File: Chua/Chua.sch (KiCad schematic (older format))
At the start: 18 parts, among them U1 TL082, U2 TL082

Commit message: assigned R and C footprint
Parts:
- C1, C2, C3: footprint (none) -> Capacitors_SMD:C_0805_HandSoldering
- R1, R2, R3, R4, R5, R6, R7, R8, R9: footprint (none) -> Resistors_SMD:R_0805_HandSoldering
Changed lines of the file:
@@
 F 0 "U2" H 9150 2550 50  0000 L CNN
 F 1 "TL082" H 9150 2150 50  0000 L CNN
-F 2 "" H 9150 2350 50  0000 C CNN
+F 2 "" H 9150 2350 50  0001 C CNN
 F 3 "" H 9150 2350 50  0000 C CNN
 	2    9150 2350
@@
 F 0 "U2" H 7900 2550 50  0000 L CNN
 F 1 "TL082" H 7900 2150 50  0000 L CNN
-F 2 "" H 7900 2350 50  0000 C CNN
+F 2 "" H 7900 2350 50  0001 C CNN
 F 3 "" H 7900 2350 50  0000 C CNN
 	1    7900 2350
@@
 F 0 "U1" H 4400 2700 50  0000 L CNN
 F 1 "TL082" H 4400 2300 50  0000 L CNN
-F 2 "" H 4400 2500 50  0000 C CNN
+F 2 "" H 4400 2500 50  0001 C CNN
 F 3 "" H 4400 2500 50  0000 C CNN
 	1    4400 2500
@@
 F 0 "U1" H 5800 3850 50  0000 L CNN
 F 1 "TL082" H 5800 3450 50  0000 L CNN
-F 2 "" H 5800 3650 50  0000 C CNN
+F 2 "" H 5800 3650 50  0001 C CNN
 F 3 "" H 5800 3650 50  0000 C CNN
 	2    5800 3650
@@
 F 0 "R4" V 8130 1850 50  0000 C CNN
 F 1 "R" V 8050 1850 50  0000 C CNN
-F 2 "" V 7980 1850 50  0000 C CNN
+F 2 "Resistors_SMD:R_0805_HandSoldering" V 7980 1850 50  0001 C CNN
 F 3 "" H 8050 1850 50  0000 C CNN
 	1    8050 1850
@@
 F 0 "R8" V 9080 1850 50  0000 C CNN
 F 1 "R" V 9000 1850 50  0000 C CNN
-F 2 "" V 8930 1850 50  0000 C CNN
+F 2 "Resistors_SMD:R_0805_HandSoldering" V 8930 1850 50  0001 C CNN
 F 3 "" H 9000 1850 50  0000 C CNN
 	1    9000 1850
@@
 F 0 "R5" V 8130 2850 50  0000 C CNN
 F 1 "R" V 8050 2850 50  0000 C CNN
-F 2 "" V 7980 2850 50  0000 C CNN
+F 2 "Resistors_SMD:R_0805_HandSoldering" V 7980 2850 50  0001 C CNN
 F 3 "" H 8050 2850 50  0000 C CNN
 	1    8050 2850
@@
 F 0 "R9" V 9130 2850 50  0000 C CNN
 F 1 "R" V 9050 2850 50  0000 C CNN
-F 2 "" V 8980 2850 50  0000 C CNN
+F 2 "Resistors_SMD:R_0805_HandSoldering" V 8980 2850 50  0001 C CNN
 F 3 "" H 9050 2850 50  0000 C CNN
 	1    9050 2850
@@
 F 0 "R6" V 8430 3200 50  0000 C CNN
 F 1 "R" V 8350 3200 50  0000 C CNN
-F 2 "" V 8280 3200 50  0000 C CNN
+F 2 "Resistors_SMD:R_0805_HandSoldering" V 8280 3200 50  0001 C CNN
 F 3 "" H 8350 3200 50  0000 C CNN
 	1    8350 3200
@@
 F 0 "R7" V 8880 3200 50  0000 C CNN
 F 1 "R" V 8800 3200 50  0000 C CNN
-F 2 "" V 8730 3200 50  0000 C CNN
+F 2 "Resistors_SMD:R_0805_HandSoldering" V 8730 3200 50  0001 C CNN
 F 3 "" H 8800 3200 50  0000 C CNN
 	1    8800 3200
@@
 F 0 "R2" V 5180 2700 50  0000 C CNN
 F 1 "R" V 5100 2700 50  0000 C CNN
-F 2 "" V 5030 2700 50  0000 C CNN
+F 2 "Resistors_SMD:R_0805_HandSoldering" V 5030 2700 50  0001 C CNN
 F 3 "" H 5100 2700 50  0000 C CNN
 	1    5100 2700
@@
 F 0 "R1" V 5180 2300 50  0000 C CNN
 F 1 "R" V 5100 2300 50  0000 C CNN
-F 2 "" V 5030 2300 50  0000 C CNN
+F 2 "Resistors_SMD:R_0805_HandSoldering" V 5030 2300 50  0001 C CNN
 F 3 "" H 5100 2300 50  0000 C CNN
 	1    5100 2300
@@
 F 0 "R3" V 5180 3450 50  0000 C CNN
 F 1 "R" V 5100 3450 50  0000 C CNN
-F 2 "" V 5030 3450 50  0000 C CNN
+F 2 "Resistors_SMD:R_0805_HandSoldering" V 5030 3450 50  0001 C CNN
 F 3 "" H 5100 3450 50  0000 C CNN
 	1    5100 3450
@@
 F 0 "RV1" H 5650 4670 50  0000 C CNN
 F 1 "POT" H 5650 4750 50  0000 C CNN
-F 2 "" H 5650 4750 50  0000 C CNN
+F 2 "" H 5650 4750 50  0001 C CNN
 F 3 "" H 5650 4750 50  0000 C CNN
 	1    5650 4750
@@
 F 0 "RV2" H 6650 1770 50  0000 C CNN
 F 1 "POT" H 6650 1850 50  0000 C CNN
-F 2 "" H 6650 1850 50  0000 C CNN
+F 2 "" H 6650 1850 50  0001 C CNN
 F 3 "" H 6650 1850 50  0000 C CNN
 	1    6650 1850
@@
 F 0 "C3" H 6925 2550 50  0000 L CNN
 F 1 "C" H 6925 2350 50  0000 L CNN
-F 2 "" H 6938 2300 50  0000 C CNN
+F 2 "Capacitors_SMD:C_0805_HandSoldering" H 6938 2300 50  0001 C CNN
 F 3 "" H 6900 2450 50  0000 C CNN
 	1    6900 2450
@@
 F 0 "C2" H 6325 2550 50  0000 L CNN
 F 1 "C" H 6325 2350 50  0000 L CNN
-F 2 "" H 6338 2300 50  0000 C CNN
+F 2 "Capacitors_SMD:C_0805_HandSoldering" H 6338 2300 50  0001 C CNN
 F 3 "" H 6300 2450 50  0000 C CNN
 	1    6300 2450
@@
 F 0 "C1" H 5125 4000 50  0000 L CNN
 F 1 "C" H 5125 3800 50  0000 L CNN
-F 2 "" H 5138 3750 50  0000 C CNN
+F 2 "Capacitors_SMD:C_0805_HandSoldering" H 5138 3750 50  0001 C CNN
 F 3 "" H 5100 3900 50  0000 C CNN
 	1    5100 3900
@@
 F 0 "BT1" H 3150 3000 50  0000 L CNN
 F 1 "Battery" H 3150 2900 50  0000 L CNN
-F 2 "" V 3050 2990 50  0000 C CNN
+F 2 "" V 3050 2990 50  0001 C CNN
 F 3 "" V 3050 2990 50  0000 C CNN
 	1    3050 2950
@@
 F 0 "BT2" H 3150 3450 50  0000 L CNN
 F 1 "Battery" H 3150 3350 50  0000 L CNN
-F 2 "" V 3050 3440 50  0000 C CNN
+F 2 "" V 3050 3440 50  0001 C CNN
 F 3 "" V 3050 3440 50  0000 C CNN
 	1    3050 3400

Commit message: something
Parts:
- removed BT1, BT2: Battery, symbol Battery
- added P1: CONN_01X03, symbol CONN_01X03
- RV1, RV2: symbol POT -> POT-RESCUE-Chua
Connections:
- wire segments 57 -> 58
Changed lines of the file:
@@
 EESchema Schematic File Version 2
+LIBS:Chua-rescue
 LIBS:power
 LIBS:device
@@
 $EndComp
 $Comp
-L POT RV1
+L POT-RESCUE-Chua RV1
 U 1 1 588EAC9A
 P 5650 4750
@@
 $EndComp
 $Comp
-L POT RV2
+L POT-RESCUE-Chua RV2
 U 1 1 588EB185
 P 6650 1850
@@
 F 3 "" H 6600 4350 50  0000 C CNN
 	1    6600 4350
-	1    0    0    -1
-$EndComp
-$Comp
-L Battery BT1
-U 1 1 588EDD7C
-P 3050 2950
-F 0 "BT1" H 3150 3000 50  0000 L CNN
-F 1 "Battery" H 3150 2900 50  0000 L CNN
-F 2 "" V 3050 2990 50  0001 C CNN
-F 3 "" V 3050 2990 50  0000 C CNN
-	1    3050 2950
-	1    0    0    -1
-$EndComp
-$Comp
-L Battery BT2
-U 1 1 588EDE8E
-P 3050 3400
-F 0 "BT2" H 3150 3450 50  0000 L CNN
-F 1 "Battery" H 3150 3350 50  0000 L CNN
-F 2 "" V 3050 3440 50  0001 C CNN
-F 3 "" V 3050 3440 50  0000 C CNN
-	1    3050 3400
 	1    0    0    -1
 $EndComp
@@
 	6900 1850 7900 1850
 Wire Wire Line
-	3050 3250 3050 3100
-Wire Wire Line
-	3050 2800 3050 2450
-Wire Wire Line
-	3700 3200 3050 3200
-Connection ~ 3050 3200
-Wire Wire Line
-	3050 3950 3050 3550
+	3050 2450 3050 3100
+Wire Wire Line
+	2900 3200 3700 3200
+Wire Wire Line
+	3050 3300 3050 3950
 Text Label 3350 2450 0    60   ~ 0
 VCC+
 Text Label 3450 3950 0    60   ~ 0
 VCC-
+Entry Wire Line
+	5700 3800 5800 3900
+$Comp
+L CONN_01X03 P1
+U 1 1 5912531E
+P 2700 3200
+F 0 "P1" H 2700 3400 50  0000 C CNN
+F 1 "CONN_01X03" V 2800 3200 50  0000 C CNN
+F 2 "" H 2700 3200 50  0000 C CNN
+F 3 "" H 2700 3200 50  0000 C CNN
+	1    2700 3200
+	-1   0    0    1
+$EndComp
+Wire Wire Line
+	3050 3100 2900 3100
+Wire Wire Line
+	3050 3300 2900 3300
 $EndSCHEMATC

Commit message: update
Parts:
- added BT1, BT2: Battery_Cell, DM_Custom:DM_9V_ON_BOARD, symbol Battery_Cell
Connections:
- net GND: now also BT1.2 (-), BT2.1 (+)
- net VCC+: now also BT1.1 (+)
- net VCC-: now also BT2.2 (-)
- net at R4.1, R8.2, U2.5 (+): now also U2.3 (+); no longer U2.2 (-)
- net at R5.1, R6.1: now also U2.2 (-); no longer U2.3 (+)
- net at C2.1, R1.1, RV2.1: now also U1.3 (+); no longer U1.2 (-)
- net at R2.2, R3.1: now also U1.2 (-), U1.6 (-); no longer U1.3 (+), U1.5 (+)
- net at C1.2, RV1.2: now also U1.5 (+); no longer U1.6 (-)
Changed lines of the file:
@@
 Connection ~ 8700 1850
 Wire Wire Line
-	8200 2250 8450 2250
-Wire Wire Line
-	8450 2250 8450 1850
+	8450 1850 8450 2450
 Connection ~ 8450 1850
 Wire Wire Line
@@
 Connection ~ 7500 2350
 Wire Wire Line
-	8350 3050 8350 2450
-Wire Wire Line
-	8350 2450 8200 2450
+	8350 2250 8350 3050
 Wire Wire Line
 	8200 2850 8350 2850
@@
 	6100 2500 5100 2500
 Connection ~ 5100 2500
-Wire Wire Line
-	4700 2400 4700 2050
-Wire Wire Line
-	4700 2050 5100 2050
 Connection ~ 5100 2050
-Wire Wire Line
-	4700 2600 4700 2950
-Wire Wire Line
-	4700 2950 5100 2950
 Wire Wire Line
 	5100 2850 5100 3300
@@
 	4100 3650 5100 3650
 Connection ~ 5100 3650
-Wire Wire Line
-	5500 3750 5500 4200
-Wire Wire Line
-	5500 4200 5100 4200
 Connection ~ 5100 4200
-Wire Wire Line
-	5500 3550 5500 3200
-Wire Wire Line
-	5500 3200 5100 3200
 Connection ~ 5100 3200
 Wire Wire Line
@@
 Text Label 3450 3950 0    60   ~ 0
 VCC-
-Entry Wire Line
-	5700 3800 5800 3900
 $Comp
 L CONN_01X03 P1
@@
 F 0 "P1" H 2700 3400 50  0000 C CNN
 F 1 "CONN_01X03" V 2800 3200 50  0000 C CNN
-F 2 "" H 2700 3200 50  0000 C CNN
+F 2 "" H 2700 3200 50  0001 C CNN
 F 3 "" H 2700 3200 50  0000 C CNN
 	1    2700 3200
@@
 Wire Wire Line
 	3050 3300 2900 3300
+Wire Wire Line
+	8200 2250 8350 2250
+Wire Wire Line
+	8450 2450 8200 2450
+Wire Wire Line
+	4700 2600 4850 2600
+Wire Wire Line
+	4850 2600 4850 2050
+Wire Wire Line
+	4700 2400 4750 2400
+Wire Wire Line
+	4750 2400 4750 2950
+Wire Wire Line
+	4750 2950 5100 2950
+Wire Wire Line
+	4850 2050 5100 2050
+Wire Wire Line
+	5400 3200 5400 3750
+Wire Wire Line
+	5400 3750 5500 3750
+Wire Wire Line
+	5100 3200 5400 3200
+Wire Wire Line
+	5500 3550 5350 3550
+Wire Wire Line
+	5350 3550 5350 4200
+Wire Wire Line
+	5350 4200 5100 4200
+$Comp
+L Battery_Cell BT1
+U 1 1 591479F0
+P 3300 3000
+F 0 "BT1" H 3400 3100 50  0000 L CNN
+F 1 "Battery_Cell" H 3400 3000 50  0000 L CNN
+F 2 "DM_Custom:DM_9V_ON_BOARD" V 3300 3060 50  0001 C CNN
+F 3 "" V 3300 3060 50  0000 C CNN
+	1    3300 3000
+	1    0    0    -1
+$EndComp
+$Comp
+L Battery_Cell BT2
+U 1 1 59147AD7
+P 3300 3500
+F 0 "BT2" H 3400 3600 50  0000 L CNN
+F 1 "Battery_Cell" H 3400 3500 50  0000 L CNN
+F 2 "DM_Custom:DM_9V_ON_BOARD" V 3300 3560 50  0001 C CNN
+F 3 "" V 3300 3560 50  0000 C CNN
+	1    3300 3500
+	1    0    0    -1
+$EndComp
+Wire Wire Line
+	3300 3100 3300 3300
+Connection ~ 3300 3200
+Wire Wire Line
+	3300 2800 3300 2450
+Connection ~ 3300 2450
+Wire Wire Line
+	3300 3600 3300 3950
+Connection ~ 3300 3950
 $EndSCHEMATC

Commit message: adding output to chua
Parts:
- added P2: CONN_01X04, Pin_Headers:Pin_Header_Straight_1x04_Pitch2.54mm, symbol CONN_01X04
- P1: footprint (none) -> Pin_Headers:Pin_Header_Straight_1x03_Pitch2.54mm
- RV1, RV2: footprint (none) -> DM_Custom:DM_POT_296
- U1, U2: footprint (none) -> DM_Custom:DM_TSSOP8
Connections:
- net GND: now also P2.4 (P4)
- net Y: now reaches C3.1, R4.2, R5.2, RV2.2, U2.1
- net Y: now also P2.2 (P2)
- net X: now reaches C2.1, R1.1, RV2.1, U1.3 (+)
- net X: now also P2.1 (P1)
- net P: now reaches R1.2, R2.1, U1.7
- net P: now also P2.3 (P3)
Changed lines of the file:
@@
 F 0 "U2" H 9150 2550 50  0000 L CNN
 F 1 "TL082" H 9150 2150 50  0000 L CNN
-F 2 "" H 9150 2350 50  0001 C CNN
+F 2 "DM_Custom:DM_TSSOP8" H 9150 2350 50  0001 C CNN
 F 3 "" H 9150 2350 50  0000 C CNN
 	2    9150 2350
@@
 F 0 "U2" H 7900 2550 50  0000 L CNN
 F 1 "TL082" H 7900 2150 50  0000 L CNN
-F 2 "" H 7900 2350 50  0001 C CNN
+F 2 "DM_Custom:DM_TSSOP8" H 7900 2350 50  0001 C CNN
 F 3 "" H 7900 2350 50  0000 C CNN
 	1    7900 2350
@@
 F 0 "U1" H 4400 2700 50  0000 L CNN
 F 1 "TL082" H 4400 2300 50  0000 L CNN
-F 2 "" H 4400 2500 50  0001 C CNN
+F 2 "DM_Custom:DM_TSSOP8" H 4400 2500 50  0001 C CNN
 F 3 "" H 4400 2500 50  0000 C CNN
 	1    4400 2500
@@
 F 0 "U1" H 5800 3850 50  0000 L CNN
 F 1 "TL082" H 5800 3450 50  0000 L CNN
-F 2 "" H 5800 3650 50  0001 C CNN
+F 2 "DM_Custom:DM_TSSOP8" H 5800 3650 50  0001 C CNN
 F 3 "" H 5800 3650 50  0000 C CNN
 	2    5800 3650
@@
 F 0 "RV1" H 5650 4670 50  0000 C CNN
 F 1 "POT" H 5650 4750 50  0000 C CNN
-F 2 "" H 5650 4750 50  0001 C CNN
+F 2 "DM_Custom:DM_POT_296" H 5650 4750 50  0001 C CNN
 F 3 "" H 5650 4750 50  0000 C CNN
 	1    5650 4750
@@
 F 0 "RV2" H 6650 1770 50  0000 C CNN
 F 1 "POT" H 6650 1850 50  0000 C CNN
-F 2 "" H 6650 1850 50  0001 C CNN
+F 2 "DM_Custom:DM_POT_296" H 6650 1850 50  0001 C CNN
 F 3 "" H 6650 1850 50  0000 C CNN
 	1    6650 1850
@@
 Connection ~ 7500 1850
 Wire Wire Line
-	6900 1700 6900 2300
+	6900 1300 6900 2300
 Connection ~ 6900 1850
 Wire Wire Line
 	5100 1850 6500 1850
 Wire Wire Line
-	6300 1850 6300 2300
+	6300 1400 6300 2300
 Wire Wire Line
 	5100 1850 5100 2150
@@
 F 0 "P1" H 2700 3400 50  0000 C CNN
 F 1 "CONN_01X03" V 2800 3200 50  0000 C CNN
-F 2 "" H 2700 3200 50  0001 C CNN
+F 2 "Pin_Headers:Pin_Header_Straight_1x03_Pitch2.54mm" H 2700 3200 50  0001 C CNN
 F 3 "" H 2700 3200 50  0000 C CNN
 	1    2700 3200
@@
 	3300 3600 3300 3950
 Connection ~ 3300 3950
+Text Label 6300 1850 0    60   ~ 0
+X
+Text Label 6900 1850 0    60   ~ 0
+Y
+Text Label 5450 2500 0    60   ~ 0
+P
+Connection ~ 5300 2500
+$Comp
+L CONN_01X04 P2
+U 1 1 59307B52
+P 6100 800
+F 0 "P2" H 6100 1050 50  0000 C CNN
+F 1 "CONN_01X04" V 6200 800 50  0000 C CNN
+F 2 "Pin_Headers:Pin_Header_Straight_1x04_Pitch2.54mm" H 6100 800 50  0001 C CNN
+F 3 "" H 6100 800 50  0000 C CNN
+	1    6100 800
+	0    -1   -1   0
+$EndComp
+$Comp
+L GND #PWR03
+U 1 1 59306F49
+P 7250 1450
+F 0 "#PWR03" H 7250 1200 50  0001 C CNN
+F 1 "GND" H 7250 1300 50  0000 C CNN
+F 2 "" H 7250 1450 50  0000 C CNN
+F 3 "" H 7250 1450 50  0000 C CNN
+	1    7250 1450
+	1    0    0    -1
+$EndComp
+Wire Wire Line
+	6250 1000 7250 1000
+Wire Wire Line
+	7250 1000 7250 1450
+Wire Wire Line
+	6900 1300 6050 1300
+Wire Wire Line
+	6050 1300 6050 1000
+Connection ~ 6900 1700
+Wire Wire Line
+	6300 1400 5950 1400
+Wire Wire Line
+	5950 1400 5950 1000
+Wire Wire Line
+	5300 2500 5300 1200
+Wire Wire Line
+	5300 1200 6150 1200
+Wire Wire Line
+	6150 1200 6150 1000
 $EndSCHEMATC

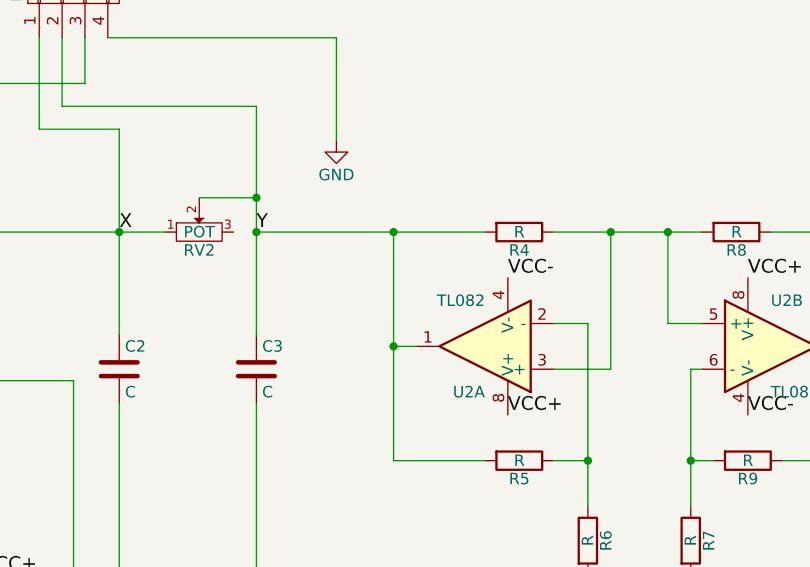
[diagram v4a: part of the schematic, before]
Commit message: fixed incorrect chua diode connection
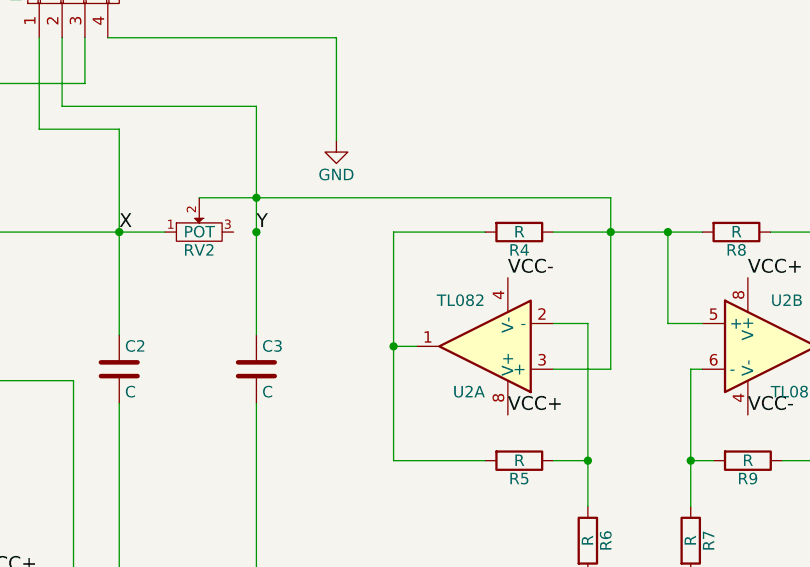
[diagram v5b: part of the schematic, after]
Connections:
- net Y: now also R4.1, R8.2, U2.3 (+), U2.5 (+); no longer R4.2, R5.2, U2.1
- new net: R4.2, R5.2, U2.1
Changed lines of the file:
@@
 Connection ~ 8700 1850
 Wire Wire Line
-	8450 1850 8450 2450
+	8450 1700 8450 2450
 Connection ~ 8450 1850
 Wire Wire Line
@@
 	6300 2600 6300 4750
 Connection ~ 6600 4100
-Connection ~ 7500 1850
 Wire Wire Line
 	6900 1300 6900 2300
@@
 Connection ~ 6300 4100
 Wire Wire Line
-	6900 1700 6650 1700
-Wire Wire Line
-	6900 1850 7900 1850
+	6650 1700 8450 1700
 Wire Wire Line
 	3050 2450 3050 3100
@@
 Wire Wire Line
 	6150 1200 6150 1000
+Wire Wire Line
+	7500 1850 7900 1850
 $EndSCHEMATC

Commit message: Clean up
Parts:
- C1, C2: value C -> 100n
- C3: value C -> 10n
- R1: value R -> 100
- R2, R3: value R -> 1K
- R4, R5: value R -> 220
- R6: value R -> 2.2K
- R7: value R -> 3.3K
- R8, R9: value R -> 22K
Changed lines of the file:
@@
 P 8050 1850
 F 0 "R4" V 8130 1850 50  0000 C CNN
-F 1 "R" V 8050 1850 50  0000 C CNN
+F 1 "220" V 8050 1850 50  0000 C CNN
 F 2 "Resistors_SMD:R_0805_HandSoldering" V 7980 1850 50  0001 C CNN
 F 3 "" H 8050 1850 50  0000 C CNN
@@
 P 9000 1850
 F 0 "R8" V 9080 1850 50  0000 C CNN
-F 1 "R" V 9000 1850 50  0000 C CNN
+F 1 "22K" V 9000 1850 50  0000 C CNN
 F 2 "Resistors_SMD:R_0805_HandSoldering" V 8930 1850 50  0001 C CNN
 F 3 "" H 9000 1850 50  0000 C CNN
@@
 P 8050 2850
 F 0 "R5" V 8130 2850 50  0000 C CNN
-F 1 "R" V 8050 2850 50  0000 C CNN
+F 1 "220" V 8050 2850 50  0000 C CNN
 F 2 "Resistors_SMD:R_0805_HandSoldering" V 7980 2850 50  0001 C CNN
 F 3 "" H 8050 2850 50  0000 C CNN
@@
 P 9050 2850
 F 0 "R9" V 9130 2850 50  0000 C CNN
-F 1 "R" V 9050 2850 50  0000 C CNN
+F 1 "22K" V 9050 2850 50  0000 C CNN
 F 2 "Resistors_SMD:R_0805_HandSoldering" V 8980 2850 50  0001 C CNN
 F 3 "" H 9050 2850 50  0000 C CNN
@@
 P 8350 3200
 F 0 "R6" V 8430 3200 50  0000 C CNN
-F 1 "R" V 8350 3200 50  0000 C CNN
+F 1 "2.2K" V 8350 3200 50  0000 C CNN
 F 2 "Resistors_SMD:R_0805_HandSoldering" V 8280 3200 50  0001 C CNN
 F 3 "" H 8350 3200 50  0000 C CNN
@@
 P 8800 3200
 F 0 "R7" V 8880 3200 50  0000 C CNN
-F 1 "R" V 8800 3200 50  0000 C CNN
+F 1 "3.3K" V 8800 3200 50  0000 C CNN
 F 2 "Resistors_SMD:R_0805_HandSoldering" V 8730 3200 50  0001 C CNN
 F 3 "" H 8800 3200 50  0000 C CNN
@@
 P 5100 2700
 F 0 "R2" V 5180 2700 50  0000 C CNN
-F 1 "R" V 5100 2700 50  0000 C CNN
+F 1 "1K" V 5100 2700 50  0000 C CNN
 F 2 "Resistors_SMD:R_0805_HandSoldering" V 5030 2700 50  0001 C CNN
 F 3 "" H 5100 2700 50  0000 C CNN
@@
 P 5100 2300
 F 0 "R1" V 5180 2300 50  0000 C CNN
-F 1 "R" V 5100 2300 50  0000 C CNN
+F 1 "100" V 5100 2300 50  0000 C CNN
 F 2 "Resistors_SMD:R_0805_HandSoldering" V 5030 2300 50  0001 C CNN
 F 3 "" H 5100 2300 50  0000 C CNN
@@
 P 5100 3450
 F 0 "R3" V 5180 3450 50  0000 C CNN
-F 1 "R" V 5100 3450 50  0000 C CNN
+F 1 "1K" V 5100 3450 50  0000 C CNN
 F 2 "Resistors_SMD:R_0805_HandSoldering" V 5030 3450 50  0001 C CNN
 F 3 "" H 5100 3450 50  0000 C CNN
@@
 P 6900 2450
 F 0 "C3" H 6925 2550 50  0000 L CNN
-F 1 "C" H 6925 2350 50  0000 L CNN
+F 1 "10n" H 6925 2350 50  0000 L CNN
 F 2 "Capacitors_SMD:C_0805_HandSoldering" H 6938 2300 50  0001 C CNN
 F 3 "" H 6900 2450 50  0000 C CNN
@@
 P 6300 2450
 F 0 "C2" H 6325 2550 50  0000 L CNN
-F 1 "C" H 6325 2350 50  0000 L CNN
+F 1 "100n" H 6325 2350 50  0000 L CNN
 F 2 "Capacitors_SMD:C_0805_HandSoldering" H 6338 2300 50  0001 C CNN
 F 3 "" H 6300 2450 50  0000 C CNN
@@
 P 5100 3900
 F 0 "C1" H 5125 4000 50  0000 L CNN
-F 1 "C" H 5125 3800 50  0000 L CNN
+F 1 "100n" H 5125 3800 50  0000 L CNN
 F 2 "Capacitors_SMD:C_0805_HandSoldering" H 5138 3750 50  0001 C CNN
 F 3 "" H 5100 3900 50  0000 C CNN
